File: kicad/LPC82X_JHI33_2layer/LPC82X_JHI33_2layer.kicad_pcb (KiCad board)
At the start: 2 copper layers, 23.6 x 23.5 mm, 24 parts, among them J1 Conn_02x09_Odd_Even, J2 Conn_02x09_Odd_Even, J3 JTAG_2X05, U1 LPC824M201JHI33, Y1 12MHz

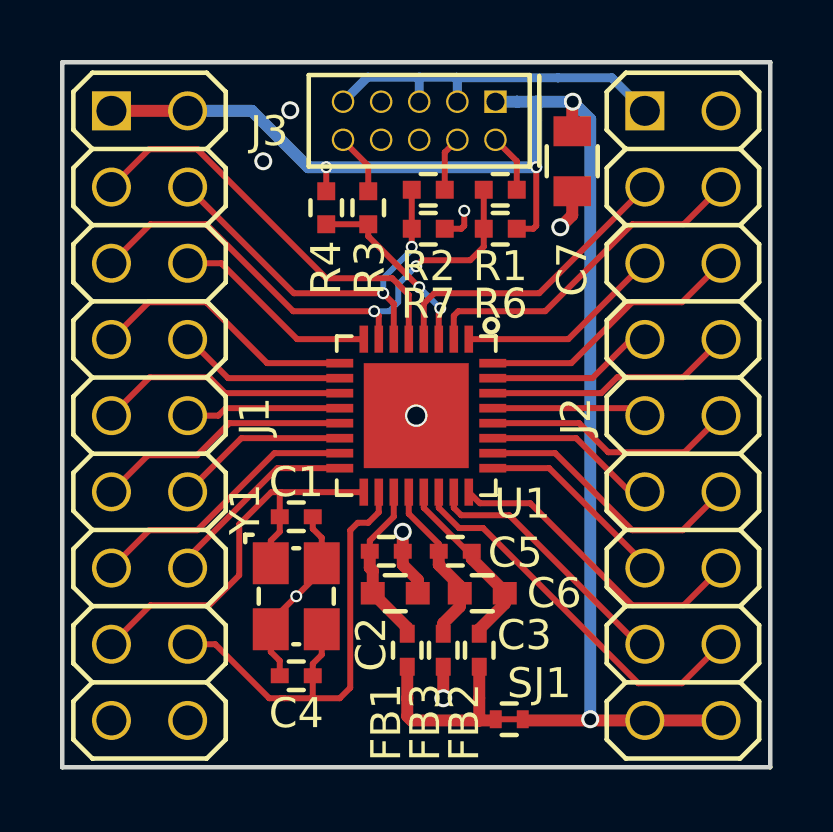
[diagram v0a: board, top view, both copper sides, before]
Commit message: fixed DRC error on PCB, fixed resistor positions, updated versionnumber
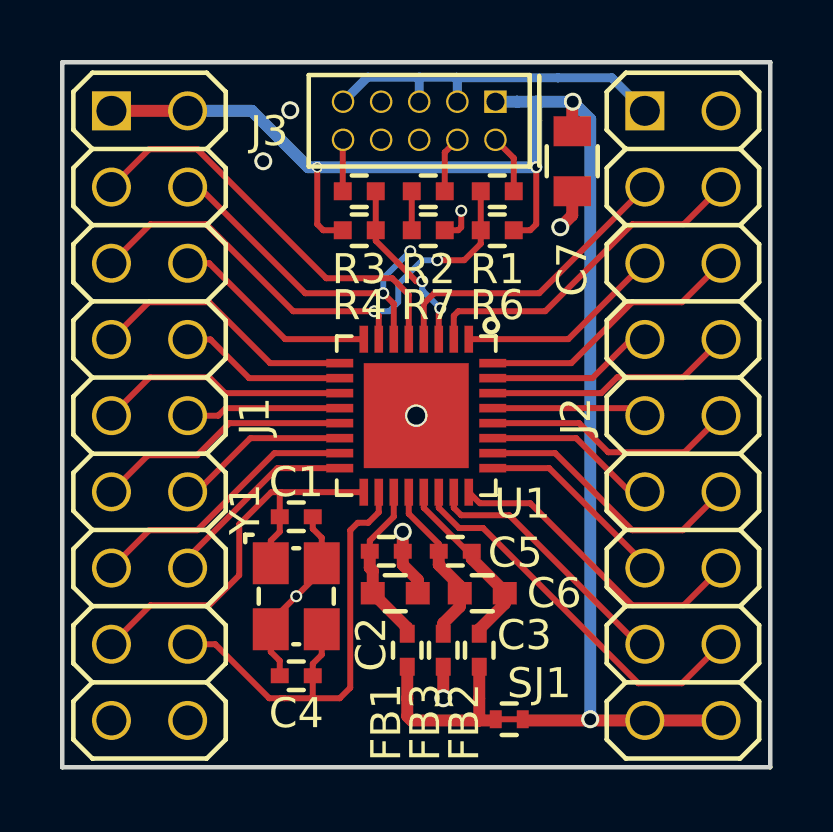
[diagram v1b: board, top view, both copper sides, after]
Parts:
- N2: value 20181122 -> 20181123
- moved R4 1.33 mm to (87.0, 100.5), turned to 0 degrees
- moved R3 0.63 mm to (87.0, 99.2), turned to 0 degrees
- moved R1 0.11 mm to (91.6, 99.2)
- moved R6 0.11 mm to (91.6, 100.5)
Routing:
- net VDD: track 51.6 -> 53.8 mm
- net /PIO0_3: track 13.5 -> 12.8 mm

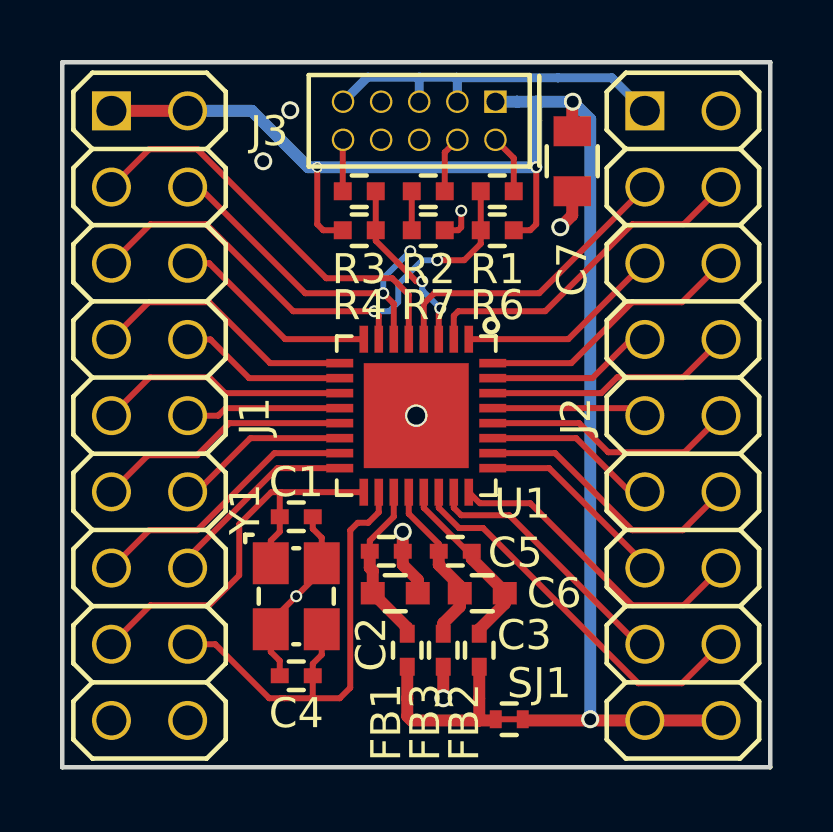
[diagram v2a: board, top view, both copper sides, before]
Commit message: updated versionnumber, fixed unrouted trace
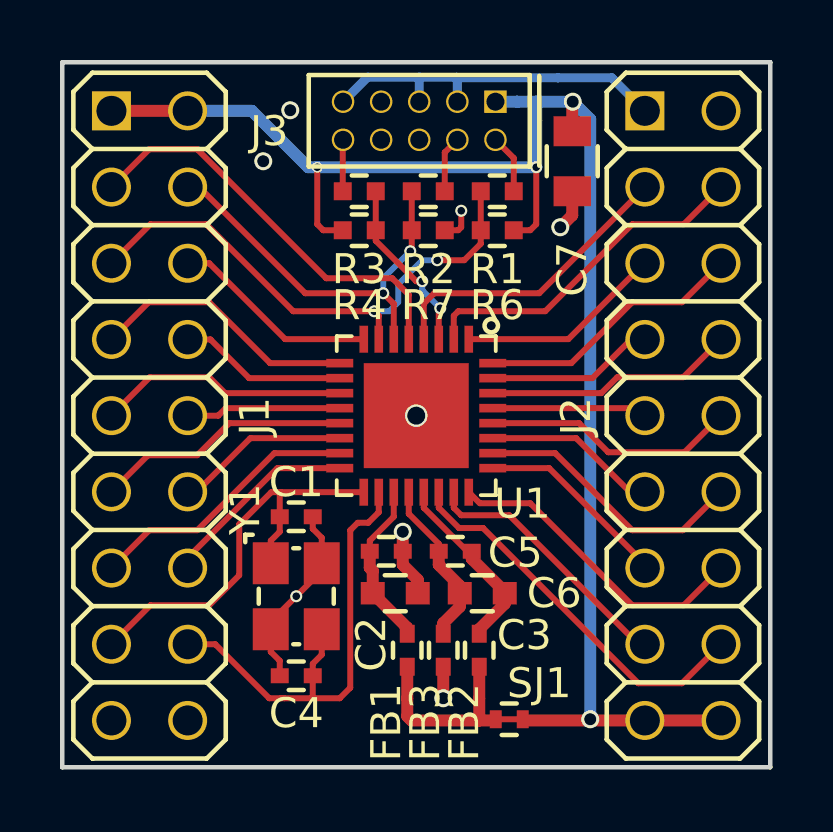
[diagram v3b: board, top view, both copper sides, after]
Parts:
- N2: value 20181123 -> 20181124
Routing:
- net /PIO0_3: track 12.8 -> 13.5 mm
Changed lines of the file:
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@@
     (thickness 1.6)
     (drawings 4)
-    (tracks 276)
+    (tracks 277)
     (zones 0)
     (modules 24)
@@
       (effects (font (size 1 1) (thickness 0.15)) (justify mirror))
     )
-    (fp_text value 20181123 (at -0.4 0.137362 270) (layer B.SilkS)
+    (fp_text value 20181124 (at -0.4 0.137362 270) (layer B.SilkS)
       (effects (font (size 1 1) (thickness 0.15)) (justify mirror))
     )
@@
   (segment (start 88.7 101.2) (end 87.8 102.1) (width 0.2) (layer B.Cu) (net 7))
   (via (at 88.7 101.2) (size 0.4) (drill 0.254) (layers F.Cu B.Cu) (net 7))
-  (segment (start 88.7 101.2) (end 88.75 101.15) (width 0.2) (layer F.Cu) (net 7))
   (segment (start 81.66 99.06) (end 81.28 99.06) (width 0.2) (layer F.Cu) (net 7))
   (segment (start 87.8 102.6) (end 85.2 102.6) (width 0.2) (layer F.Cu) (net 7))
   (segment (start 85.2 102.6) (end 81.66 99.06) (width 0.2) (layer F.Cu) (net 7))
   (segment (start 88.75 99.2) (end 88.75 100.5) (width 0.2) (layer F.Cu) (net 7))
+  (segment (start 88.75 101.15) (end 88.7 101.2) (width 0.2) (layer F.Cu) (net 7))
+  (segment (start 88.75 100.5) (end 88.75 101.15) (width 0.2) (layer F.Cu) (net 7))
   (segment (start 87.65 104.13) (end 87.65 103.35) (width 0.2) (layer F.Cu) (net 8))
   (segment (start 87.65 103.35) (end 87.5 103.2) (width 0.2) (layer F.Cu) (net 8))
